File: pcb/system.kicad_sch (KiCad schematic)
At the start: 8 parts, among them J1 USB_C_Receptacle_USB2.0_14P, U1 RP2040, U2 W25Q128JVS, U5 MB85RS1MT

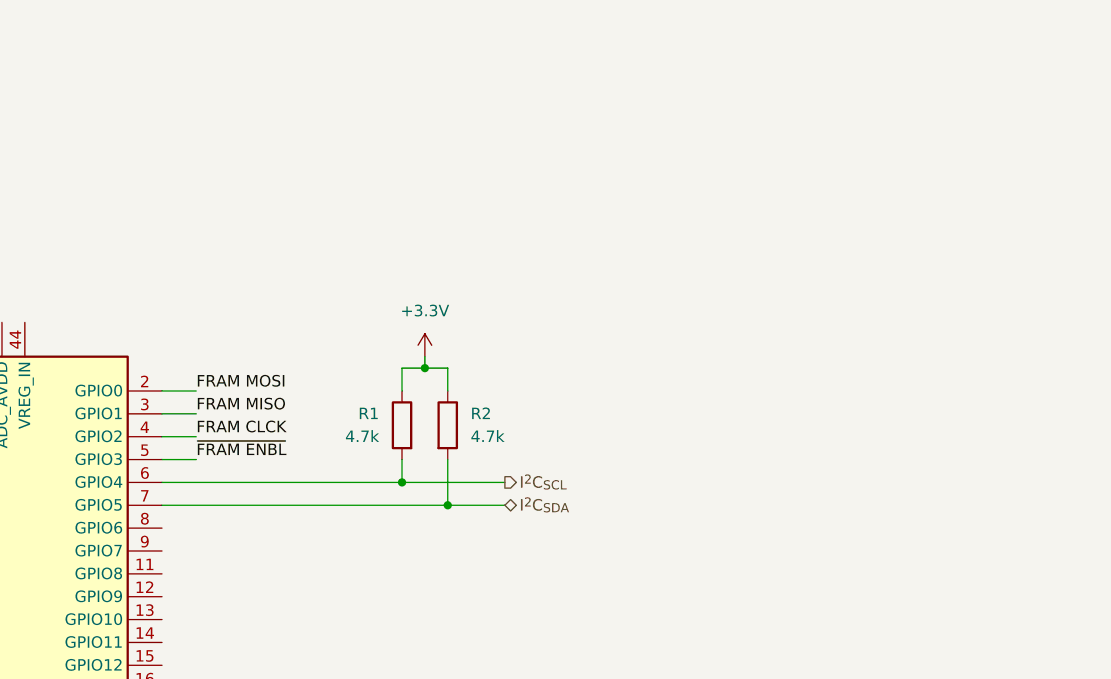
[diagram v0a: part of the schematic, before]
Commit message: chore: added pull-down on rs-485 transceiver
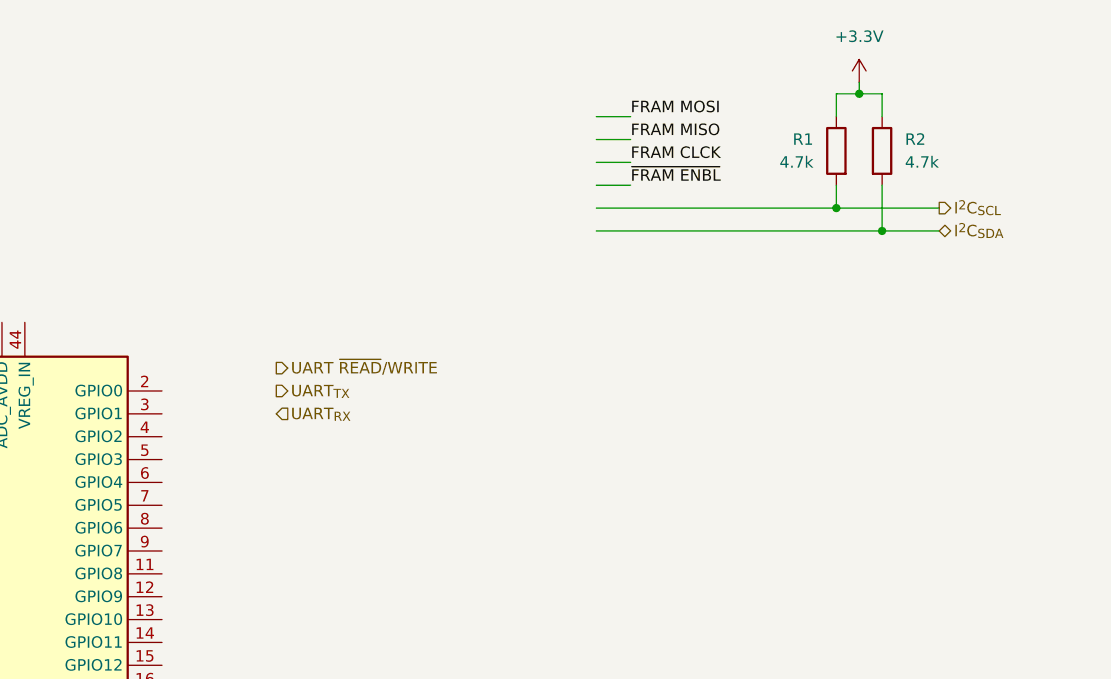
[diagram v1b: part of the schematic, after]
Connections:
- net FRAM CLCK: no longer U1.4 (GPIO2)
- net FRAM MISO: no longer U1.3 (GPIO1)
- net FRAM MOSI: no longer U1.2 (GPIO0)
- net I^{2}C_{SCL}: no longer U1.6 (GPIO4)
- net I^{2}C_{SDA}: no longer U1.7 (GPIO5)
- net ~{FRAM ENBL}: no longer U1.5 (GPIO3)
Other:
- moved on the sheet: R1, R2

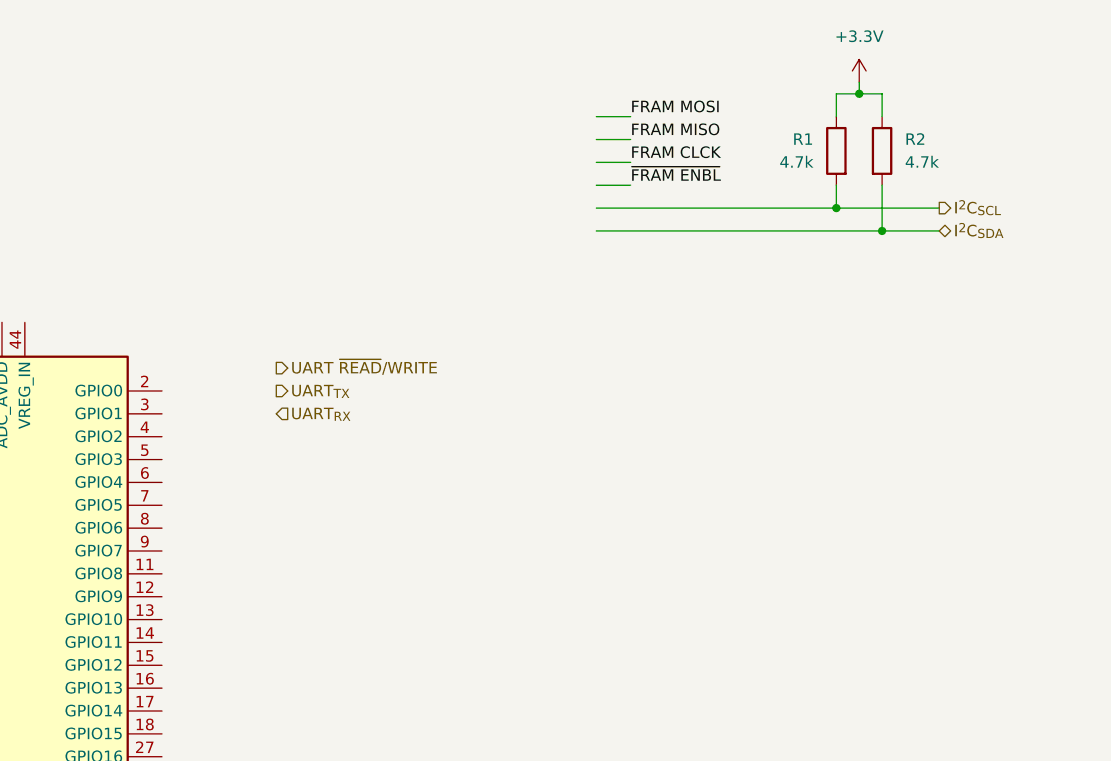
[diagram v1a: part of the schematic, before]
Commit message: feat: pin layout for I2C, SPI, and UART peripherals
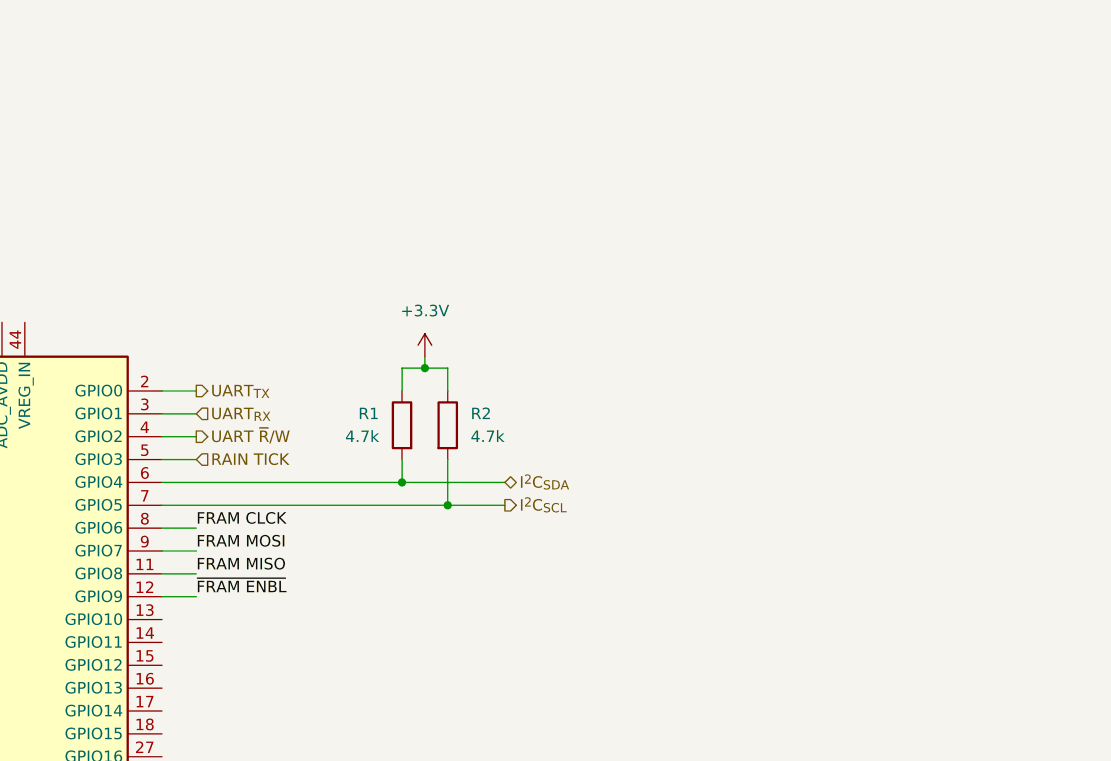
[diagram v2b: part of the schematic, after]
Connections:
- net FRAM CLCK: now also U1.8 (GPIO6)
- net FRAM MISO: now also U1.11 (GPIO8)
- net FRAM MOSI: now also U1.9 (GPIO7)
- net I^{2}C_{SCL}: now also R2.2, U1.7 (GPIO5); no longer R1.2
- net I^{2}C_{SDA}: now also R1.2, U1.6 (GPIO4); no longer R2.2
- net UART_{RX}: now also U1.3 (GPIO1)
- net UART_{TX}: now also U1.2 (GPIO0)
- net ~{FRAM ENBL}: now also U1.12 (GPIO9)
- net UART ~{R}/W: now reaches U1.4 (GPIO2)
- net RAIN TICK: now reaches U1.5 (GPIO3)
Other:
- moved on the sheet: R1, R2

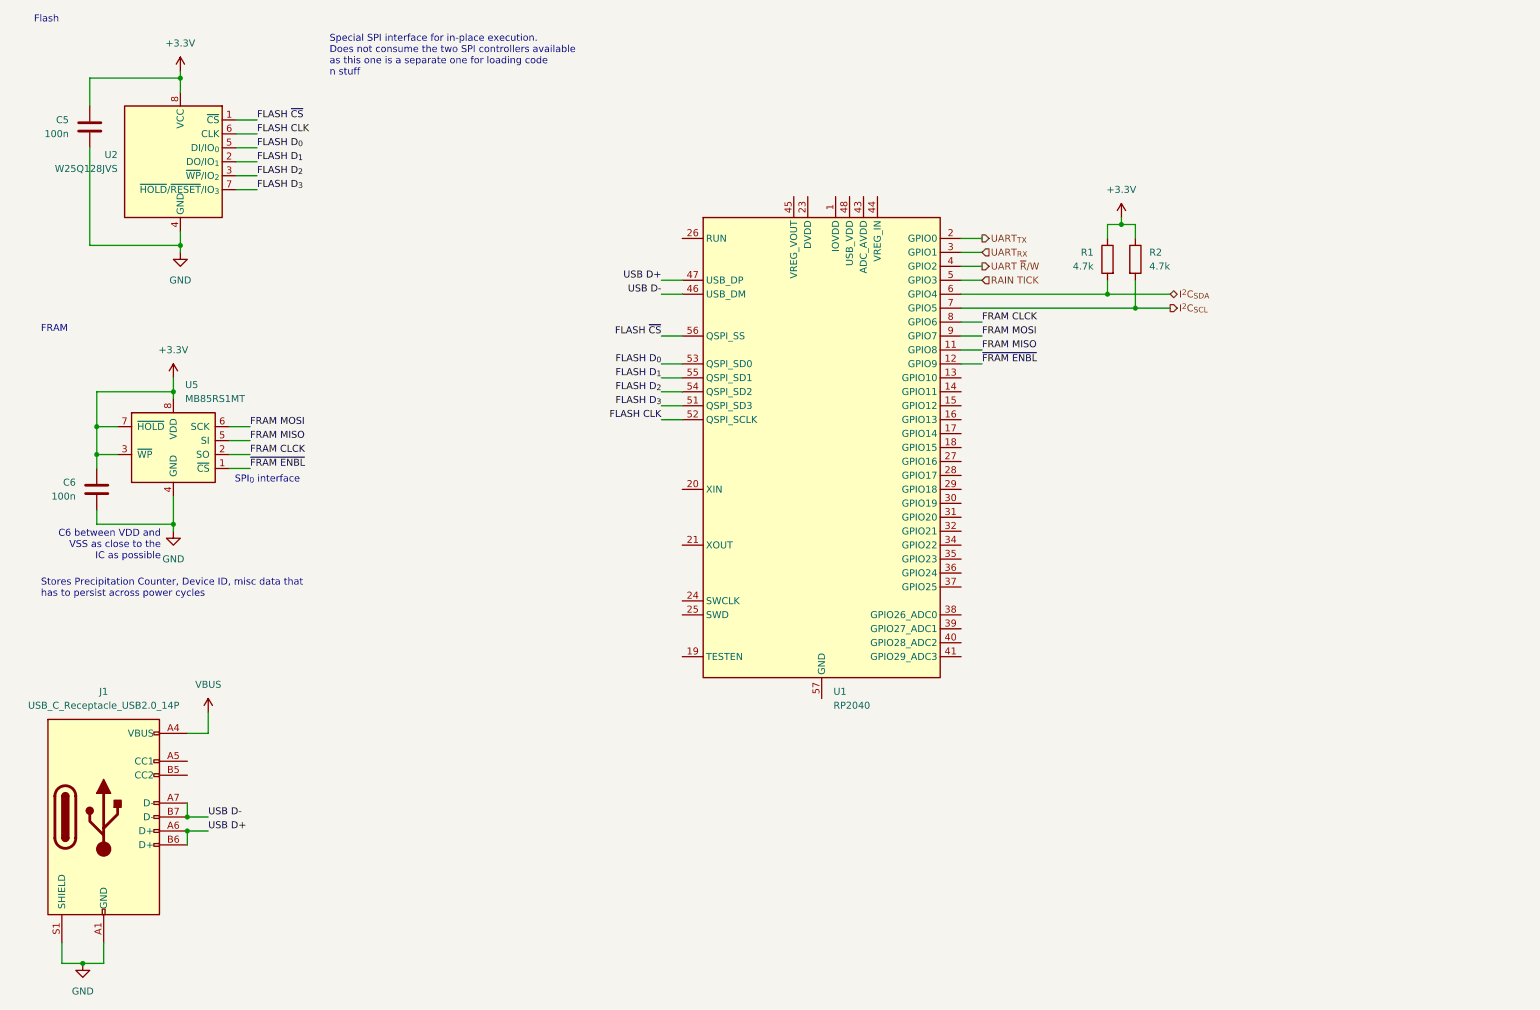
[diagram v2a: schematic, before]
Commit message: feat: RP2040 power rails
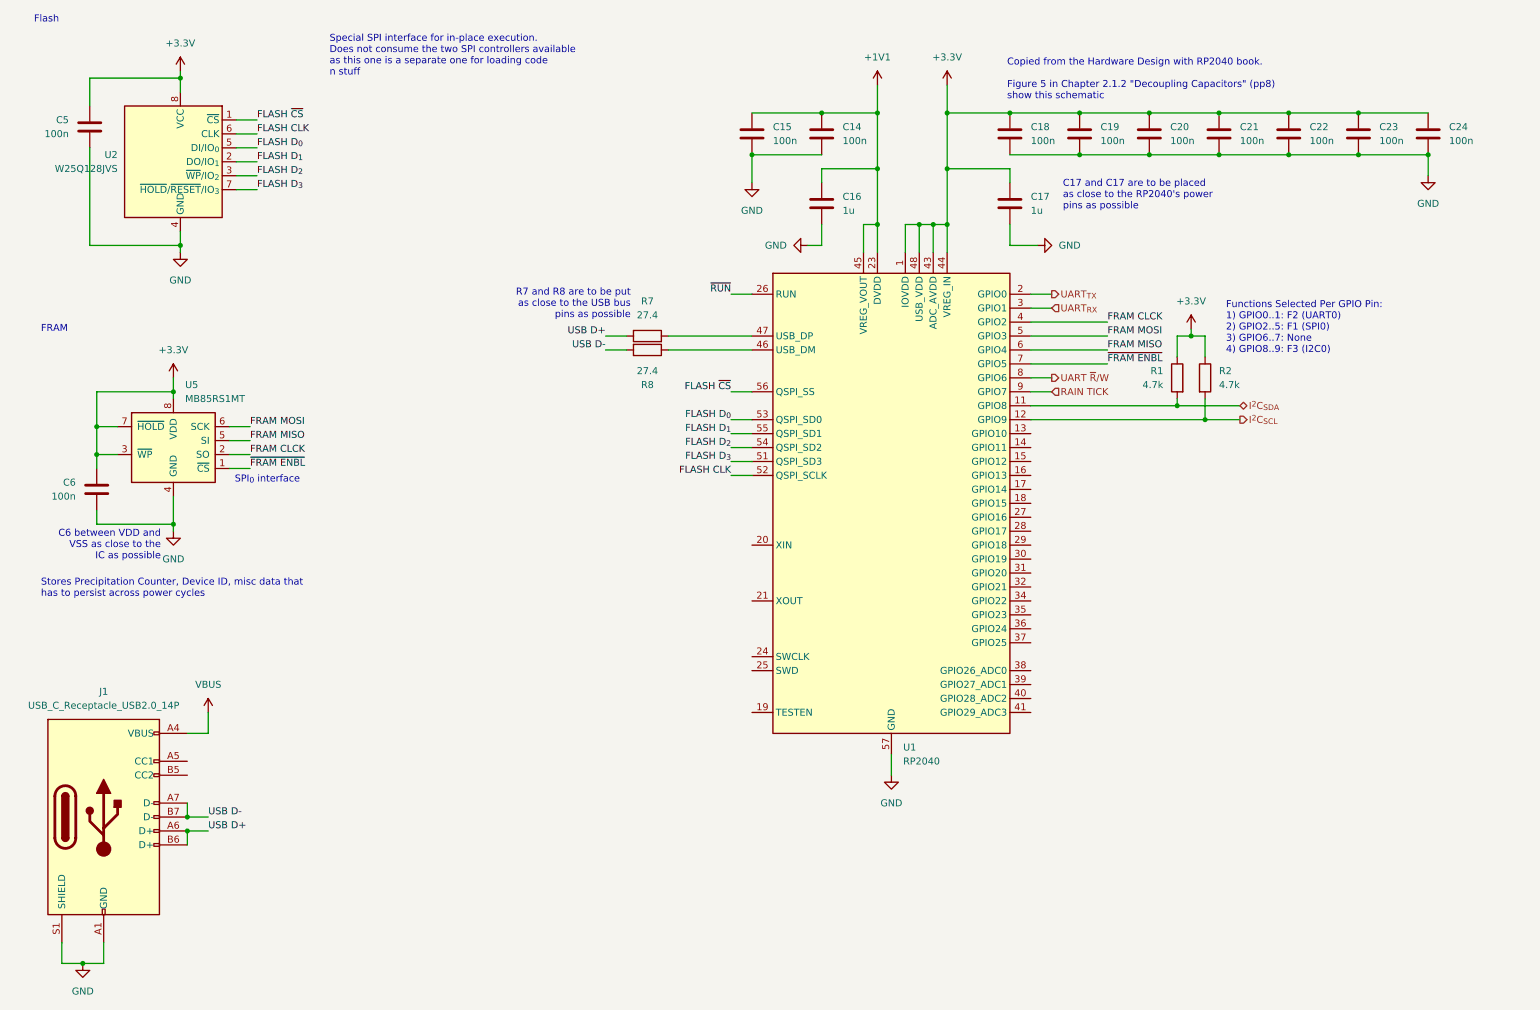
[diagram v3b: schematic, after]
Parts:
- added C14, C15, C18, C19, C20, C21, C22, C23, C24: 100n, symbol Device:C
- added C16, C17: 1u, symbol Device:C
- added R7, R8: 27.4, symbol Device:R
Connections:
- net +3.3V: now also U1.1 (IOVDD), U1.10 (IOVDD), U1.22 (IOVDD), U1.33 (IOVDD), U1.42 (IOVDD), U1.43 (ADC_AVDD), U1.44 (VREG_IN), U1.48 (USB_VDD), U1.49 (IOVDD), C17.1, C18.1, C19.1, C20.1, C21.1, C22.1, C23.1, C24.1
- net FRAM CLCK: now also U1.4 (GPIO2); no longer U1.8 (GPIO6)
- net FRAM MISO: now also U1.6 (GPIO4); no longer U1.11 (GPIO8)
- net FRAM MOSI: now also U1.5 (GPIO3); no longer U1.9 (GPIO7)
- net GND: now also U1.57 (GND), C14.2, C15.2, C16.2, C17.2, C18.2, C19.2, C20.2, C21.2, C22.2, C23.2, C24.2
- net I^{2}C_{SCL}: now also U1.12 (GPIO9); no longer U1.7 (GPIO5)
- net I^{2}C_{SDA}: now also U1.11 (GPIO8); no longer U1.6 (GPIO4)
- net RAIN TICK: now also U1.9 (GPIO7); no longer U1.5 (GPIO3)
- net UART ~{R}/W: now also U1.8 (GPIO6); no longer U1.4 (GPIO2)
- net USB D+: now also R7.1; no longer U1.47 (USB_DP)
- net USB D-: now also R8.2; no longer U1.46 (USB_DM)
- net ~{FRAM ENBL}: now also U1.7 (GPIO5); no longer U1.12 (GPIO9)
- net +1V1: now reaches U1.23 (DVDD), U1.50 (DVDD)
- net +1V1: now also U1.45 (VREG_VOUT), C14.1, C15.1, C16.1
- net ~{RUN}: now reaches U1.26 (RUN)
- new net: R8.1, U1.46 (USB_DM)
- new net: R7.2, U1.47 (USB_DP)
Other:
- note added: "C17 and C17 are to be placed as close to the RP2040's power pins as possible"
- note added: "Copied from the Hardware Design with RP2040 book. Figure 5 in Chapter 2.1.2 "Decoupling Capacitors" (pp8) show this schematic"
- note added: "Functions Selected Per GPIO Pin: 1) GPIO0..1: F2 (UART0) 2) GPIO2..5: F1 (SPI0) 3) GPIO6..7: None 4) GPIO8..9: F3 (I2C0)"
- note added: "R7 and R8 are to be put as close to the USB bus pins as possible"
- moved on the sheet: R1, R2, U1

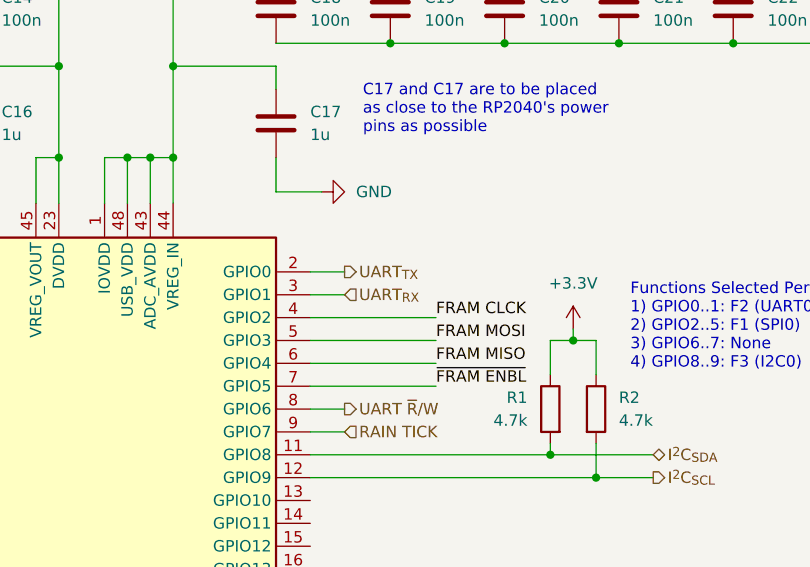
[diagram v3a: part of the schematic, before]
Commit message: feat: PMS7003 sensor
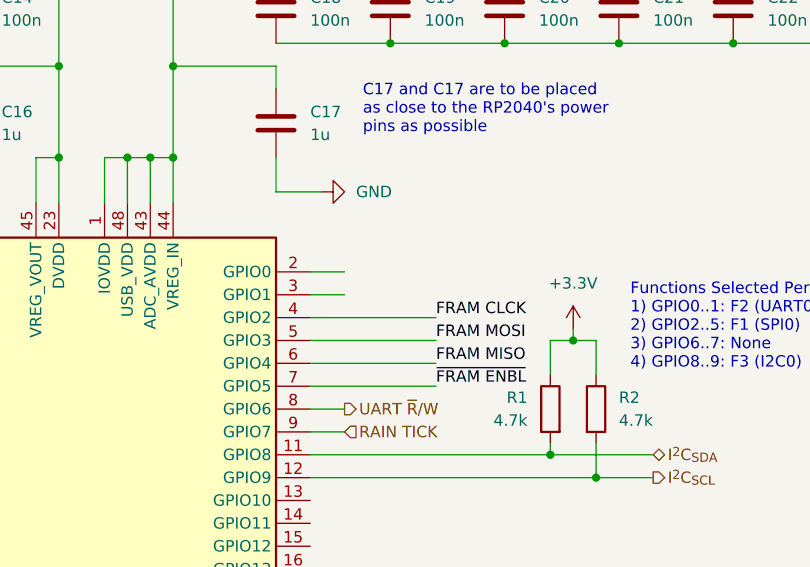
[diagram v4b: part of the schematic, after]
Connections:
- net UART_{RX}: no longer names the net of U1.3 (GPIO1)
- net UART_{TX}: no longer names the net of U1.2 (GPIO0)
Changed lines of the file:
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@@
-		)
-	)
-	(hierarchical_label "UART_{RX}"
-		(shape input)
-		(at 204.47 71.12 0)
-		(effects
-			(font
-				(size 1.27 1.27)
-			)
-			(justify left)
 		)
 	)
@@
 		(effects
 			(font
-				(size 1.27 1.27)
-			)
-			(justify left)
-		)
-	)
-	(hierarchical_label "UART_{TX}"
-		(shape output)
-		(at 204.47 68.58 0)
-		(effects
-			(font

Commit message: feat: finalized usb receptacle
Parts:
- removed J1: USB_C_Receptacle_USB2.0_14P, symbol Connector:USB_C_Receptacle_USB2.0_14P
- added J1: USB_C_Receptacle_USB2.0_16P, Connector_USB:USB_C_Receptacle_G-Switch_GT-USB-7010ASV, symbol Connector:USB_C_Receptacle_USB2.0_16P
- added R11, R12: 5.1k, symbol Device:R
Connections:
- net GND: now also J1.A1 (GND), J1.A12 (GND), J1.B1 (GND), J1.B12 (GND), J1.S1 (SHIELD), R11.2, R12.2
- net USB D+: now also J1.A6 (D+), J1.B6 (D+)
- net USB D-: now also J1.A7 (D-), J1.B7 (D-)
- net VBUS: now also J1.A4 (VBUS), J1.A9 (VBUS), J1.B4 (VBUS), J1.B9 (VBUS)
- new net: J1.B5 (CC2), R12.1
- new net: J1.A5 (CC1), R11.1
- no-connect marks 0 -> 2
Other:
- note added: "90 ohm impedance go here"
- note added: "R11 and R12 close to the connector"

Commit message: feat: SWD
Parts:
- added J6: Conn_01x04, symbol Connector_Generic:Conn_01x04
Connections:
- net +3.3V: now also J6.1 (Pin_1)
- net GND: now also J6.4 (Pin_4)
- net at U1.24 (SWCLK): now also J6.2 (Pin_2)
- net at U1.25 (SWD): now also J6.3 (Pin_3)
- no-connect marks 2 -> 3
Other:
- note added: "Serial Debug Interface"
